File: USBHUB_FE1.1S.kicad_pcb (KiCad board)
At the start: 2 copper layers, 306.6 x 132.1 mm, 179 parts

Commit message: Routed, Rev1
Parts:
- removed 10K (x5), 1K (x7), 2K7 (x4), 330R (x15), FUSE (x4): R_1206_3216Metric, Resistor_SMD:R_1206_3216Metric
- removed 10uF (x3): CP_Radial_D5.0mm_P2.50mm, Capacitor_THT:CP_Radial_D5.0mm_P2.50mm
- removed 10uF (x6): CP_Elec_4x5.4, Capacitor_SMD:CP_Elec_4x5.4
- removed 10uF (x6): C_1206_3216Metric_Pad1.33x1.80mm_HandSolder, Capacitor_SMD:C_1206_3216Metric_Pad1.33x1.80mm_HandSolder
- removed 10uF (x3), 22pF (x9): C_Disc_D3.8mm_W2.6mm_P2.50mm, Capacitor_THT:C_Disc_D3.8mm_W2.6mm_P2.50mm
- removed 12MHz (x4): Resonator_SMD_Murata_CSTxExxV-3Pin_3.0x1.1mm, Crystal:Resonator_SMD_Murata_CSTxExxV-3Pin_3.0x1.1mm
- removed 12MHz (x3): Crystal_HC50_Vertical, Crystal:Crystal_HC50_Vertical
- removed 2.7K (x3): R_Axial_DIN0207_L6.3mm_D2.5mm_P10.16mm_Horizontal, Resistor_THT:R_Axial_DIN0207_L6.3mm_D2.5mm_P10.16mm_Horizontal
- removed ? (x3): , 
- removed BTN (x2), FUSE (x3), RESET (x2), TEST (x2): SolderJumper-2_P1.3mm_Open_Pad1.0x1.5mm, Jumper:SolderJumper-2_P1.3mm_Open_Pad1.0x1.5mm
- removed FE1.1s (x7): SOP64P600X175-28N, SOP64P600X175-28N
- removed G***: LOGO, LOGO
- removed PORT1 (x5), PORT2 (x5), PORT3 (x5), PORT4 (x5), PWR (x5), REF** (x10): LED_PLCC_2835_Handsoldering, LED_SMD:LED_PLCC_2835_Handsoldering
- removed REF** (x9): PinSocket_1x04_P2.54mm_Vertical, Connector_PinSocket_2.54mm:PinSocket_1x04_P2.54mm_Vertical
- removed REF** (x4): PinHeader_1x01_P2.54mm_Vertical, Connector_PinHeader_2.54mm:PinHeader_1x01_P2.54mm_Vertical
- removed REF** (x2): PinHeader_1x03_P2.54mm_Vertical, Connector_PinHeader_2.54mm:PinHeader_1x03_P2.54mm_Vertical
- removed RESET (x4): SW_Push_1P1T_NO_6x6mm_H9.5mm, Button_Switch_SMD:SW_Push_1P1T_NO_6x6mm_H9.5mm
- removed SW (x2): SW_PUSH_6mm, Button_Switch_THT:SW_PUSH_6mm
- removed TEST (x2): SolderWirePad_1x01_SMD_1x2mm, Connector_Wire:SolderWirePad_1x01_SMD_1x2mm
- removed USB1 (x4), USB_0 (x2), USB_H, USB_S1, USB_S2: USB_A_CNCTech_1001-011-01101_Horizontal, Connector_USB:USB_A_CNCTech_1001-011-01101_Horizontal
- removed USB1 (x4), USB2 (x4), USB3 (x4), USB4 (x4), USB5 (x2), USB_0 (x2): USB_A_Molex_67643_Horizontal, Connector_USB:USB_A_Molex_67643_Horizontal
- added C1: 100µF 16V, Capacitor_SMD:CP_Elec_6.3x5.4, F.Cu at (121.4, 121.3)
- added C2: 100µF 16V, Capacitor_SMD:CP_Elec_6.3x5.4, F.Cu at (103.8, 121.3)
- added C3: 100µF 16V, Capacitor_SMD:CP_Elec_6.3x5.4, F.Cu at (75.2, 121.5)
- added C4: 100µF 16V, Capacitor_SMD:CP_Elec_6.3x5.4, F.Cu at (58.8, 121.5)
- added C5: 10uF16V, Capacitor_SMD:C_0805_2012Metric, F.Cu at (98.2, 117.7)
- added C6: 10uF16V, Capacitor_SMD:C_0805_2012Metric, F.Cu at (93.7, 111.0)
- added C7: 10uF16V, Capacitor_SMD:C_0805_2012Metric, F.Cu at (98.6, 110.9)
- added D1: RED, LED_SMD:LED_0805_2012Metric, F.Cu at (83.4, 110.6)
- added D2: GREEN, LED_SMD:LED_0805_2012Metric, F.Cu at (74.0, 114.1)
- added D3: GREEN, LED_SMD:LED_0805_2012Metric, F.Cu at (70.8, 114.1)
- added D4: GREEN, LED_SMD:LED_0805_2012Metric, F.Cu at (67.2, 114.1)
- added D5: GREEN, LED_SMD:LED_0805_2012Metric, F.Cu at (63.7, 114.0)
- added FB1: FerriteBead, Inductor_SMD:L_0805_2012Metric, F.Cu at (115.4, 121.3)
- added FB2: FerriteBead, Inductor_SMD:L_0805_2012Metric, F.Cu at (111.2, 120.9)
- added FB3: FerriteBead, Inductor_SMD:L_0805_2012Metric, F.Cu at (69.1, 120.3)
- added FB4: FerriteBead, Inductor_SMD:L_0805_2012Metric, F.Cu at (52.1, 120.3)
- added FB5: FerriteBead, Inductor_SMD:L_0805_2012Metric, F.Cu at (111.2, 118.7)
- added FID1: Fiducial, Fiducial:Fiducial_0.5mm_Mask1.5mm, F.Cu at (45.5, 125.0)
- added FID2: Fiducial, Fiducial:Fiducial_0.5mm_Mask1.5mm, F.Cu at (79.0, 108.5)
- added FID3: Fiducial, Fiducial:Fiducial_0.5mm_Mask1.5mm, F.Cu at (131.0, 127.5)
- added H1: MountingHole_Pad, MountingHole:MountingHole_3.2mm_M3_DIN965_Pad_TopBottom, F.Cu at (129.5, 110.5)
- added H2: MountingHole_Pad, MountingHole:MountingHole_3.2mm_M3_DIN965_Pad_TopBottom, F.Cu at (47.0, 110.5)
- added H3: MountingHole_Pad, MountingHole:MountingHole_3.2mm_M3_DIN965_Pad_TopBottom, F.Cu at (47.0, 135.0)
- added H4: MountingHole_Pad, MountingHole:MountingHole_3.2mm_M3_DIN965_Pad_TopBottom, F.Cu at (129.5, 135.0)
- added H5: MountingHole_Pad, MountingHole:MountingHole_3.2mm_M3_DIN965_Pad_TopBottom, F.Cu at (88.0, 135.0)
- added J5: Conn_01x04_Socket, Connector_JST:JST_PH_S4B-PH-SM4-TB_1x04-1MP_P2.00mm_Horizontal, F.Cu at (107.4, 112.3)
- added J6: USB-A-S-X-X-TH, lib:SAMTEC_USB-A-S-X-X-TH, F.Cu at (118.0, 130.0)
- added J7: USB-A-S-X-X-TH, lib:SAMTEC_USB-A-S-X-X-TH, F.Cu at (100.5, 130.0)
- added J8: USB-A-S-X-X-TH, lib:SAMTEC_USB-A-S-X-X-TH, F.Cu at (75.9, 130.0)
- added J9: USB-A-S-X-X-TH, lib:SAMTEC_USB-A-S-X-X-TH, F.Cu at (58.4, 130.0)
- added R1: 330, Resistor_SMD:R_0805_2012Metric, F.Cu at (81.0, 114.1)
- added R2: 2K7, Resistor_SMD:R_0805_2012Metric, F.Cu at (88.1, 110.7)
- added R3: 2K7, Resistor_SMD:R_0805_2012Metric, F.Cu at (96.1, 117.7)
- added R4: 330, Resistor_SMD:R_0805_2012Metric, F.Cu at (74.6, 111.0)
- added R5: 330, Resistor_SMD:R_0805_2012Metric, F.Cu at (68.1, 111.0)
- added U1: FE1.1s, Package_SO:SSOP-28_3.9x9.9mm_P0.635mm, F.Cu at (89.9, 115.9)
- added Y1: Crystal_GND24, Crystal:Crystal_SMD_3225-4Pin_3.2x2.5mm, F.Cu at (82.7, 119.1)
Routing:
- net (no net): track 4684.0 -> 0.00 mm, vias 21 -> 0
- net +5V: track 0.00 -> 96.8 mm, vias 0 -> 4
- net GND: track 0.00 -> 42.2 mm, vias 0 -> 48
- net Net-(J6-VCC): track 0.00 -> 36.4 mm
- net /D4-: track 0.00 -> 35.1 mm
- net /D4+: track 0.00 -> 34.5 mm
- net Net-(D2-A): track 0.00 -> 32.7 mm
- net /D1+: track 0.00 -> 32.0 mm
- net /D1-: track 0.00 -> 32.0 mm
- net Net-(J7-VCC): track 0.00 -> 23.2 mm, vias 0 -> 2
- net Net-(U1-LED2): track 0.00 -> 21.9 mm, vias 0 -> 2
- net /D3-: track 0.00 -> 21.4 mm
- net /D3+: track 0.00 -> 20.8 mm
- net /DU-: track 0.00 -> 19.9 mm
- net /DU+: track 0.00 -> 19.9 mm
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- added copper zone on B.Cu, net GND
- added copper zone on F.Cu, net GND
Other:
- board size 306.6 x 132.1 mm -> 89.5 x 32.5 mm
- board text added: "<- To host. Do not hotplug this side!"
- board text added: "Fork of TONIKILLER 10000 USB HUB V3.0 on github"
- board text added: "P. Areny 2026 Rev1"
- board text added: "USB2.0 Hub"
- board text removed: "+"
- board text removed: "-"
- board text removed: "Future mistakes: USB PORT GND CASE POWER(all ports needed to work), power pins..., clk??? , BUS POWERING??,"
- board text removed: "TONIKILLER 10000"
- board text removed: "TONIKILLER 10000 USB HUB V2.3"
- board text removed: "TONIKILLER 10000 USB HUB V2.7"
- board text removed: "TONIKILLER 10000 USB HUB V3.0"
- board text removed: "USB HUB"
- board text removed: "V2.0"
- board text removed: "V2.5"

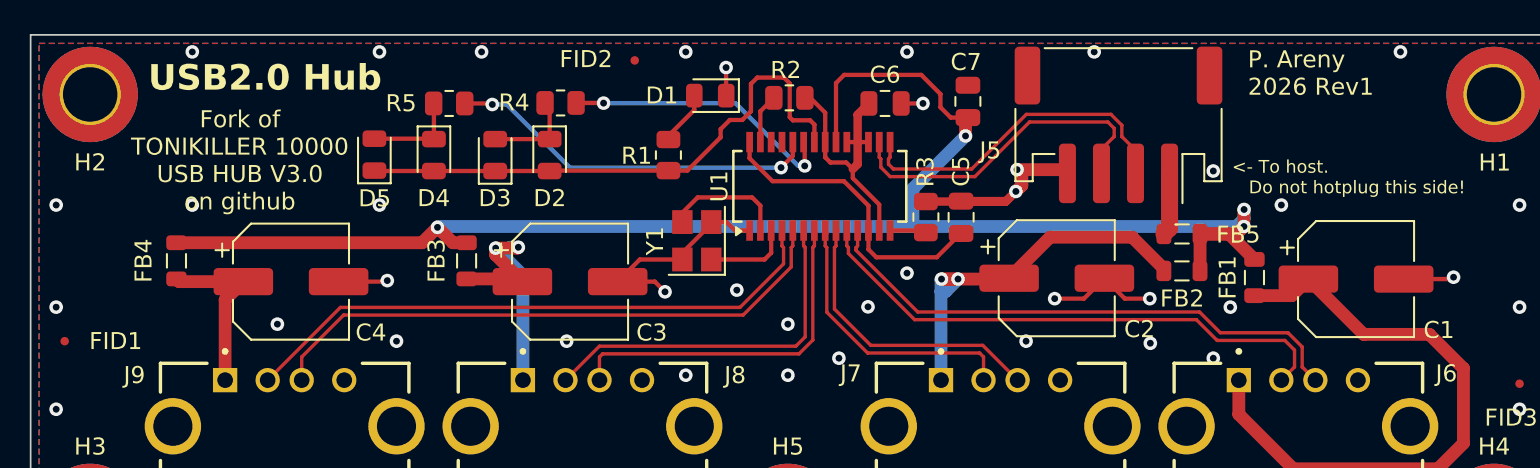
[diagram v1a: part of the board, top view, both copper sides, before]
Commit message: Reordering the leds on the board.
They should be in the same order as the ports.
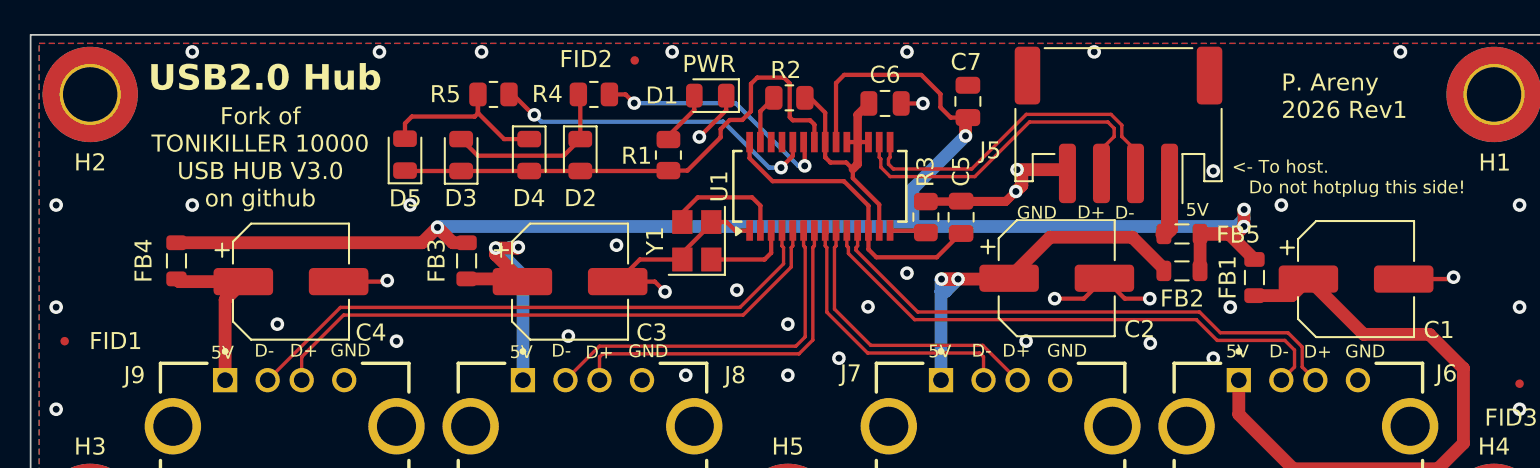
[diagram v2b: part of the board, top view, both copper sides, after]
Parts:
- moved D4 5.60 mm to (72.8, 114.1)
- moved R5 2.66 mm to (70.7, 110.5)
- moved R4 2.02 mm to (76.6, 110.5)
- moved D3 2.00 mm to (68.8, 114.1)
- moved D2 1.80 mm to (75.8, 114.1)
- moved D5 1.80 mm to (65.5, 114.0)
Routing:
- net Net-(D4-K): track 5.61 -> 11.3 mm
- net Net-(D2-K): track 5.44 -> 10.5 mm
- net Net-(U1-LED2): track 21.9 -> 19.5 mm
- net Net-(D2-A): track 32.7 -> 30.9 mm
- net Net-(U1-LED1/EESCL): track 16.4 -> 14.6 mm
- net GND: track 42.2 -> 43.7 mm, vias 48 -> 49
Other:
- board text added: "5V"
- board text added: "D+"
- board text added: "D-"
- board text added: "GND"
- board text added: "PWR"

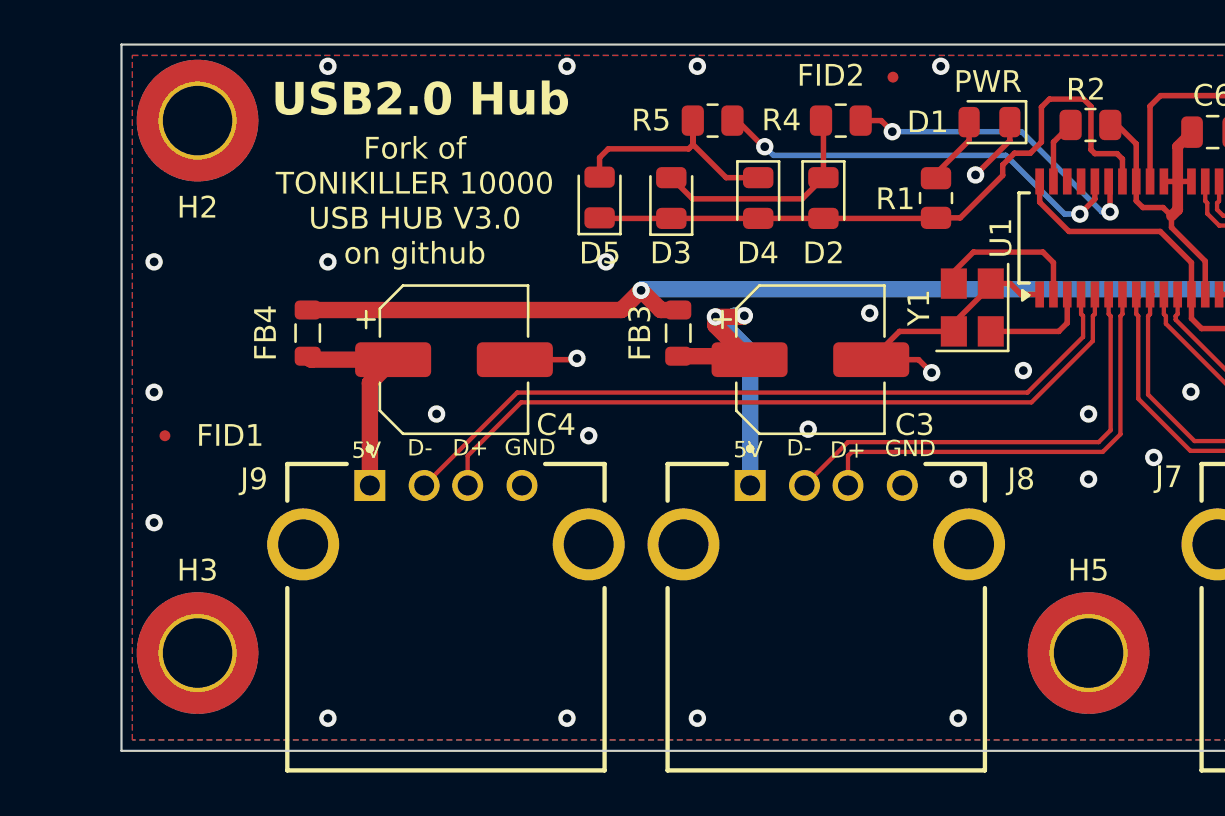
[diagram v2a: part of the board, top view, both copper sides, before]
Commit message: Puts port on the side
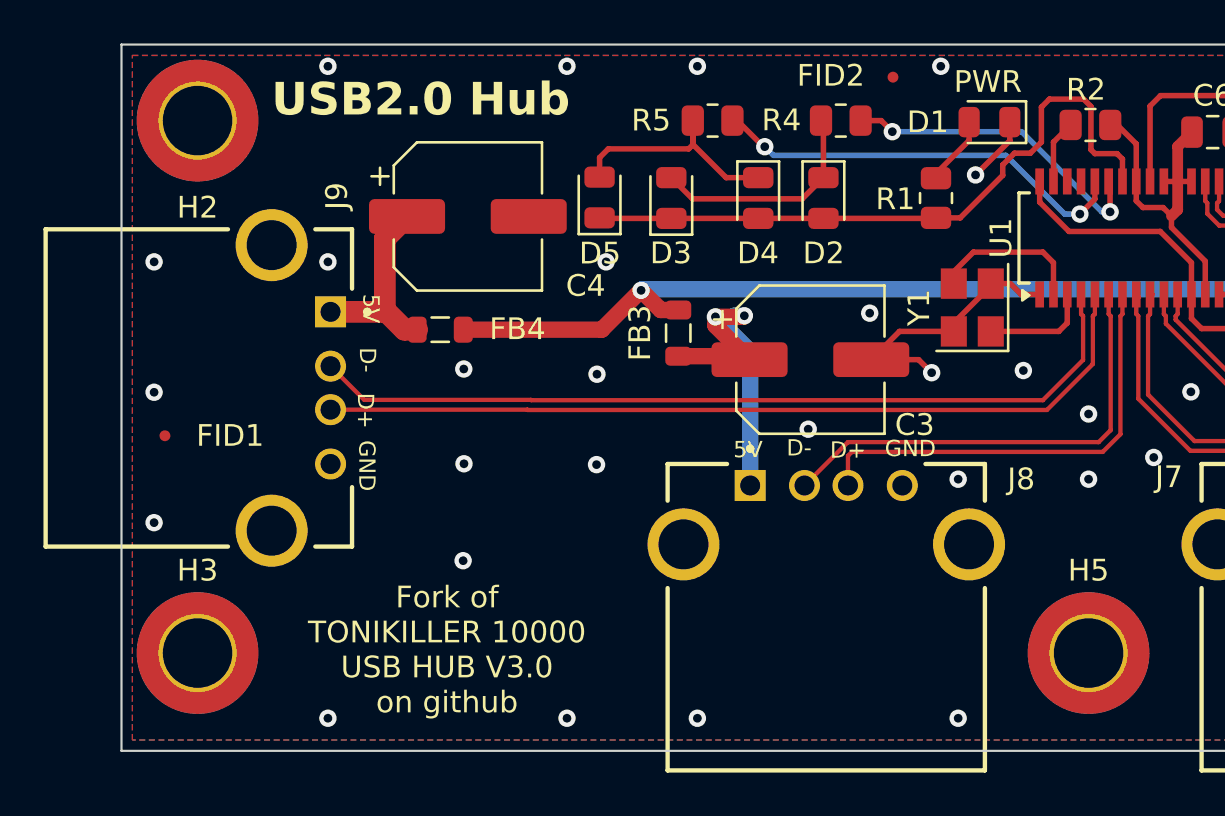
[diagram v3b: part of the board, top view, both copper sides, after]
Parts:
- moved J9 10.8 mm to (50.4, 122.8), turned to -90 degrees
- moved C4 6.62 mm to (59.4, 114.9)
- moved FB4 6.10 mm to (58.2, 120.1), turned to 180 degrees
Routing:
- net +5V: track 96.8 -> 90.0 mm
- net /D4+: track 34.5 -> 39.2 mm
- net /D4-: track 35.1 -> 39.1 mm
- net GND: track 43.7 -> 40.8 mm, vias 49 -> 51
- net Net-(J9-VCC): track 10.2 -> 9.17 mm
